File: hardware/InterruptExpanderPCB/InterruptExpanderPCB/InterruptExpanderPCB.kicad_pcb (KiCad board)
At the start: 4 copper layers, 41 parts, among them J1 Conn_01x06_Pin, J2 Conn_01x08_Pin, J3 Conn_01x08_Pin, U1 ATTINY85-20SU, U2 SN74HC251PWR, U3 SN74HC590ADT, U4 SN74HCT138PWRE4

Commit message: finished finally compiling assembly
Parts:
- added U5: 74AHC1G08, Package_TO_SOT_SMD:SOT-353_SC-70-5_Handsoldering, F.Cu at (135.2, 71.8)
- moved C12 86.6 mm to (76.5, 107.0)
- moved R16 86.4 mm to (83.1, 110.0)
- moved R15 85.9 mm to (83.1, 107.0)
- moved R14 83.8 mm to (81.0, 96.5)
- moved C11 83.5 mm to (74.9, 95.1)
- moved R12 80.1 mm to (81.0, 82.5)
- moved R13 79.9 mm to (84.5, 93.0)
- moved C10 76.6 mm to (79.0, 84.5)
- moved R1 74.5 mm to (82.0, 40.0)
- moved R9 74.0 mm to (80.5, 74.5)
- moved R3 73.1 mm to (82.0, 48.0)
- moved R2 73.0 mm to (84.5, 40.0)
- moved R5 72.8 mm to (81.5, 54.5)
- moved R11 72.4 mm to (83.0, 84.5)
- moved R7 72.2 mm to (82.0, 60.5)
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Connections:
- U3 pad 10: Net-(U3-QG) -> Net-(U3-~{CCLR})

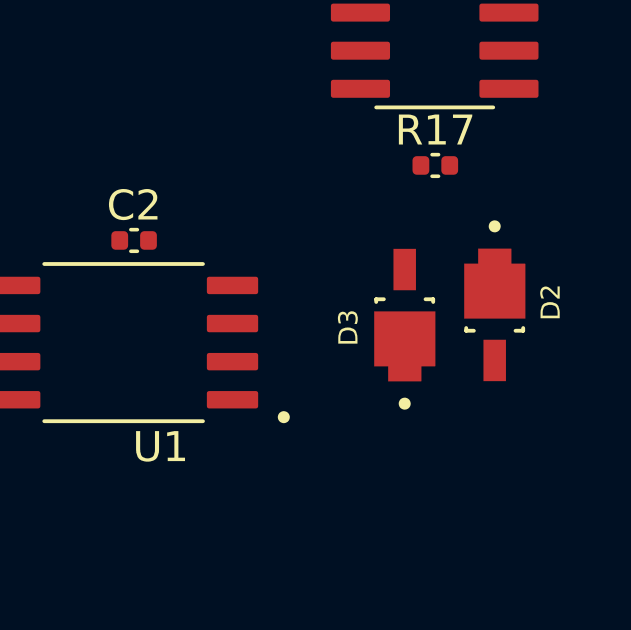
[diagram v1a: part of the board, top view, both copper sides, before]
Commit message: Fixed an issue identified with hardware for shared clock read and write functions. Fixed issue with SPI loop on firmware
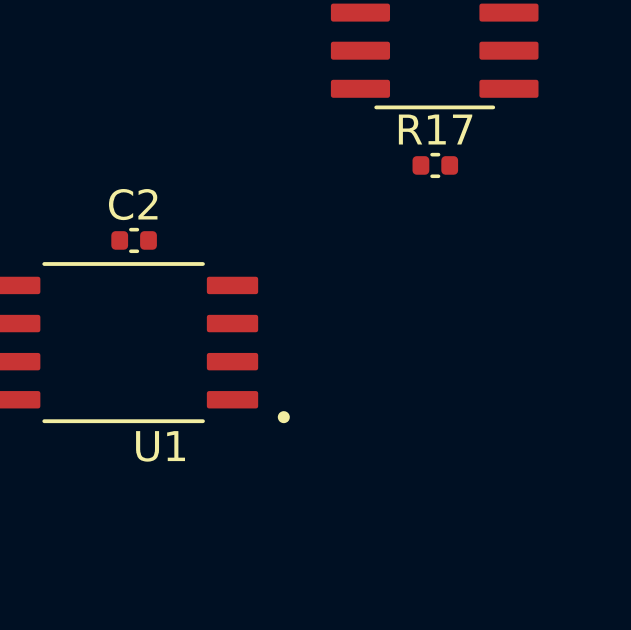
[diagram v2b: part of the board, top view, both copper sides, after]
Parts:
- removed D2, D3: D, InterrupterLibrary:RF01128
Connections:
- J1 pad 2: Net-(J1-Pin_2) -> unconnected-(J1-Pin_2-Pad2)
- R17 pad 1: Net-(D2-K) -> Net-(U1-PB1)
- U1 pad 2: Net-(D2-A) -> Net-(U1-PB3)
- U1 pad 6: Net-(J1-Pin_2) -> Net-(U1-PB1)
- U2 pad 6: Net-(D3-A) -> Net-(U1-PB3)
- U3 pad 11: Net-(D2-K) -> Net-(U1-PB1)
- U3 pad 13: Net-(D2-K) -> Net-(U1-PB1)
